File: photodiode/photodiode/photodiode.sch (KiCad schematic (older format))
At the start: 3 parts, among them J1 Conn_01x03_Male

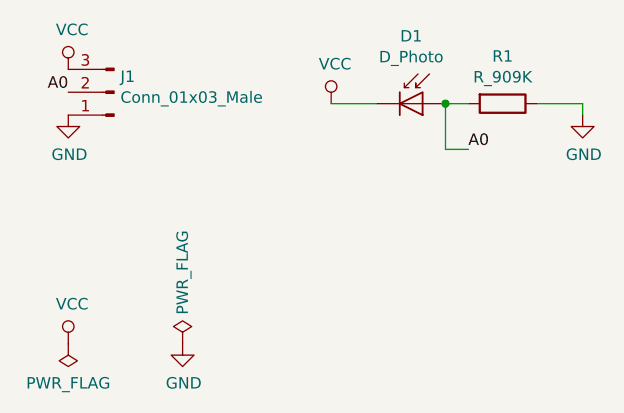
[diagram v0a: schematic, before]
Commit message: Add voltage divider to photodiode circuit/pcb
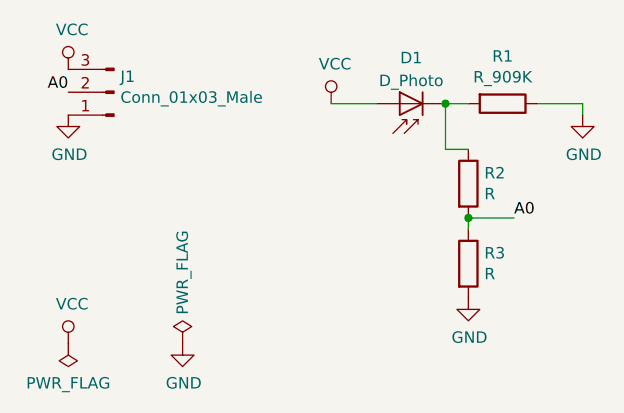
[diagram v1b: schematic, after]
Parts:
- added R2, R3: R, Resistor_SMD:R_0805_2012Metric, symbol Device:R
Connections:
- net A0: now also R2.2, R3.1; no longer D1.2 (A), R1.2
- net GND: now also R3.2
- net VCC: now also D1.2 (A); no longer D1.1 (K)
- new net: D1.1 (K), R1.2, R2.1
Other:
- moved on the sheet: D1
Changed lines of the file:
@@
 L Device:D_Photo D1
 U 1 1 5DC9C9B2
-P 2400 1900
-F 0 "D1" H 2350 2195 50  0000 C CNN
-F 1 "D_Photo" H 2350 2104 50  0000 C CNN
-F 2 "Connector_PinHeader_2.54mm:PinHeader_1x02_P2.54mm_Vertical" H 2350 1900 50  0001 C CNN
-F 3 "~" H 2350 1900 50  0001 C CNN
-	1    2400 1900
-	1    0    0    -1
+P 2300 1900
+F 0 "D1" H 2250 1700 50  0000 C CNN
+F 1 "D_Photo" H 2250 1800 50  0000 C CNN
+F 2 "Connector_PinHeader_2.54mm:PinHeader_1x02_P2.54mm_Vertical" H 2250 1900 50  0001 C CNN
+F 3 "~" H 2250 1900 50  0001 C CNN
+	1    2300 1900
+	-1   0    0    1
 $EndComp
 $Comp
@@
 	3100 1900 2900 1900
 Wire Wire Line
-	2200 1900 2000 1900
-Wire Wire Line
 	3100 1900 3100 1950
 Wire Wire Line
@@
 Wire Wire Line
 	2500 1900 2500 2100
-Connection ~ 2500 1900
-Text Label 2600 2100 0    50   ~ 0
+Text Label 2800 2400 0    50   ~ 0
 A0
 $Comp
@@
 	1    0    0    -1
 $EndComp
+Wire Wire Line
+	2000 1900 2200 1900
+Connection ~ 2500 1900
+$Comp
+L Device:R R2
+U 1 1 5DDEA59D
+P 2600 2250
+F 0 "R2" H 2670 2296 50  0000 L CNN
+F 1 "R" H 2670 2205 50  0000 L CNN
+F 2 "Resistor_SMD:R_0805_2012Metric" V 2530 2250 50  0001 C CNN
+F 3 "~" H 2600 2250 50  0001 C CNN
+	1    2600 2250
+	1    0    0    -1
+$EndComp
+$Comp
+L Device:R R3
+U 1 1 5DDEA697
+P 2600 2600
+F 0 "R3" H 2670 2646 50  0000 L CNN
+F 1 "R" H 2670 2555 50  0000 L CNN
+F 2 "Resistor_SMD:R_0805_2012Metric" V 2530 2600 50  0001 C CNN
+F 3 "~" H 2600 2600 50  0001 C CNN
+	1    2600 2600
+	1    0    0    -1
+$EndComp
+$Comp
+L power:GND #PWR0101
+U 1 1 5DDEA749
+P 2600 2750
+F 0 "#PWR0101" H 2600 2500 50  0001 C CNN
+F 1 "GND" H 2605 2577 50  0000 C CNN
+F 2 "" H 2600 2750 50  0001 C CNN
+F 3 "" H 2600 2750 50  0001 C CNN
+	1    2600 2750
+	1    0    0    -1
+$EndComp
+Wire Wire Line
+	2600 2450 2600 2400
+Wire Wire Line
+	2600 2400 2800 2400
+Connection ~ 2600 2400
 $EndSCHEMATC
